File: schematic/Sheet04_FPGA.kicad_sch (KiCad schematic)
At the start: 6 parts

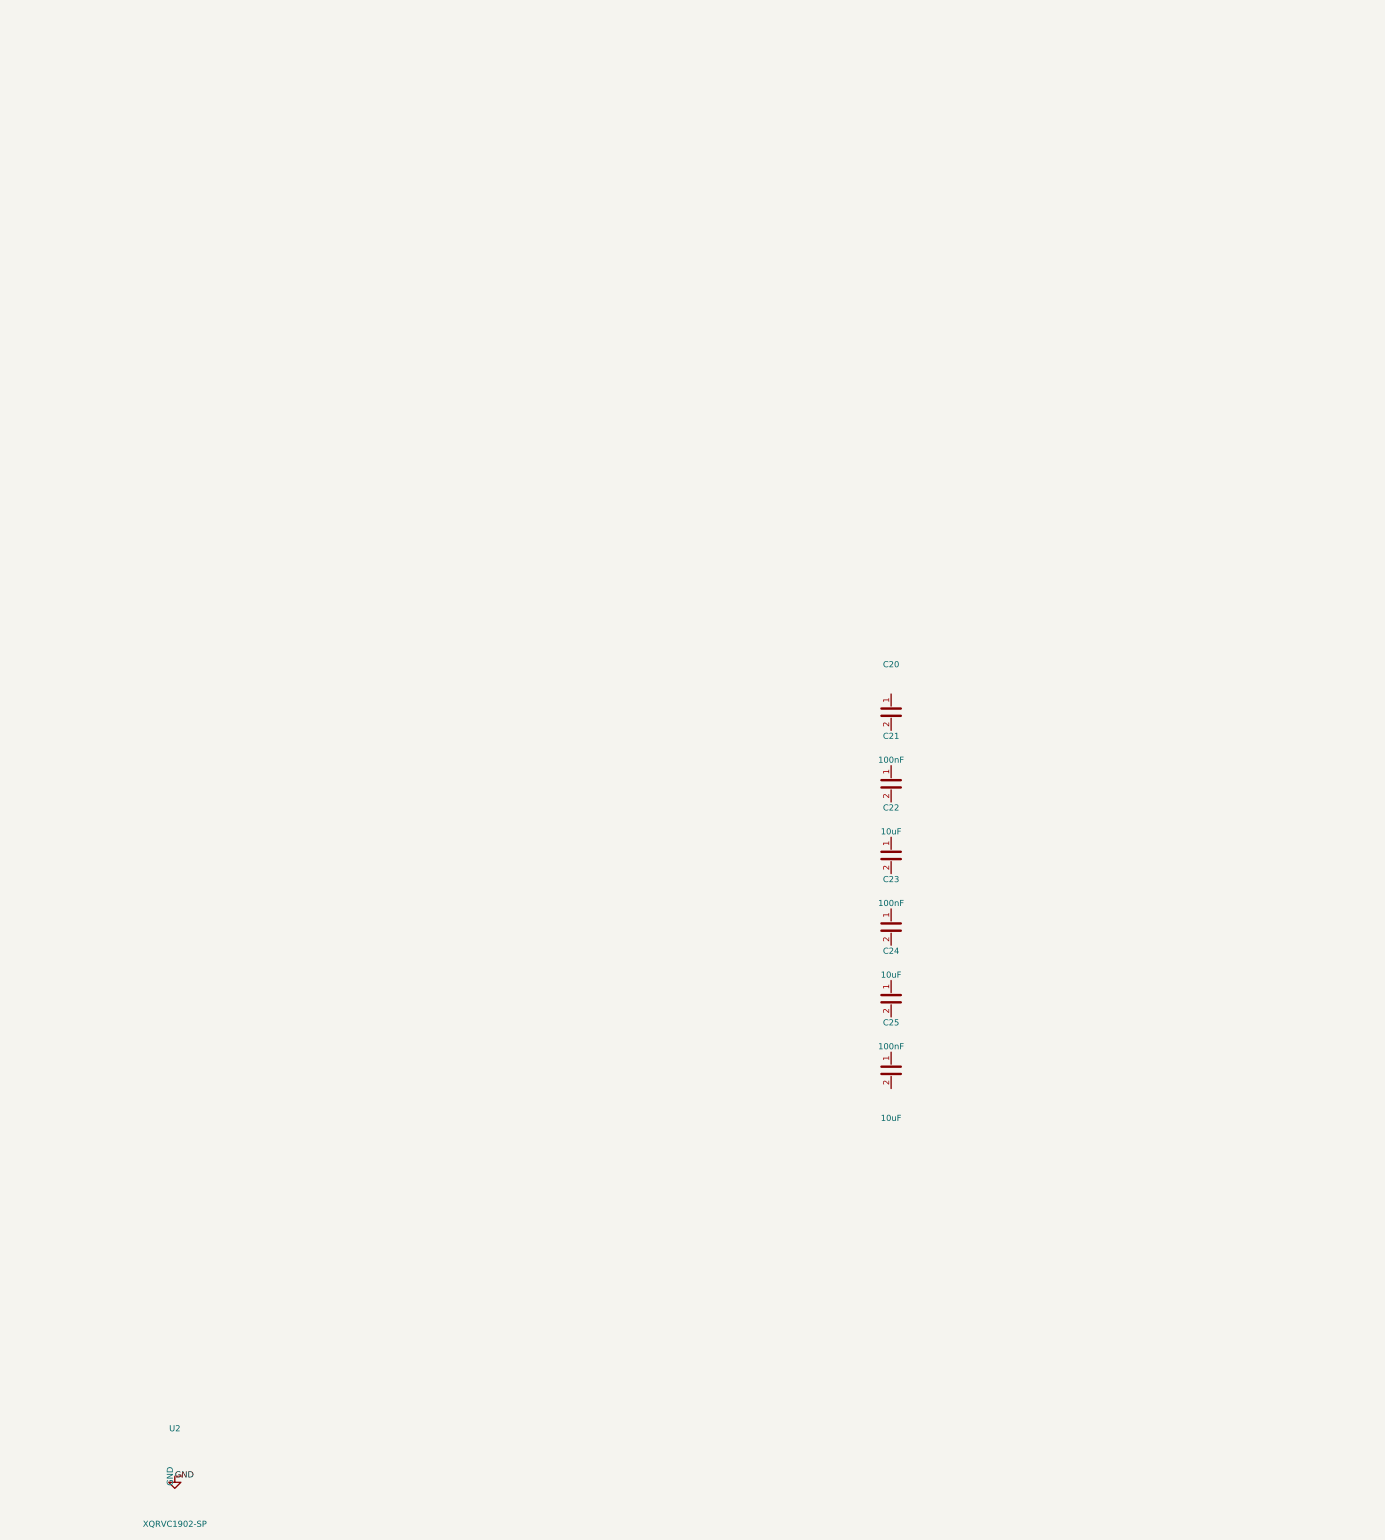
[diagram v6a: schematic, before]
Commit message: fix: isolate ISL70003ASEH buck pins, fix LMX_SYNC collision, NC pins, connector pin names
- ISL70003ASEH pins now use ref prefix (U6_LX1 vs U7_LX1) to prevent shorts
- Buck SYNC pins separated from LMX_SYNC (power sync ≠ PLL sync)
- NC pins properly skipped (unconnected)
- Connector PIN_1..PIN_6 use ref prefix (J1_PIN_1 vs J2_PIN_1)
- Fixed annotation warnings in Sheet13 (C_dev→C125, R_dev→R74, U_TPS7H→U14)
- Regenerated all PDFs and SVGs
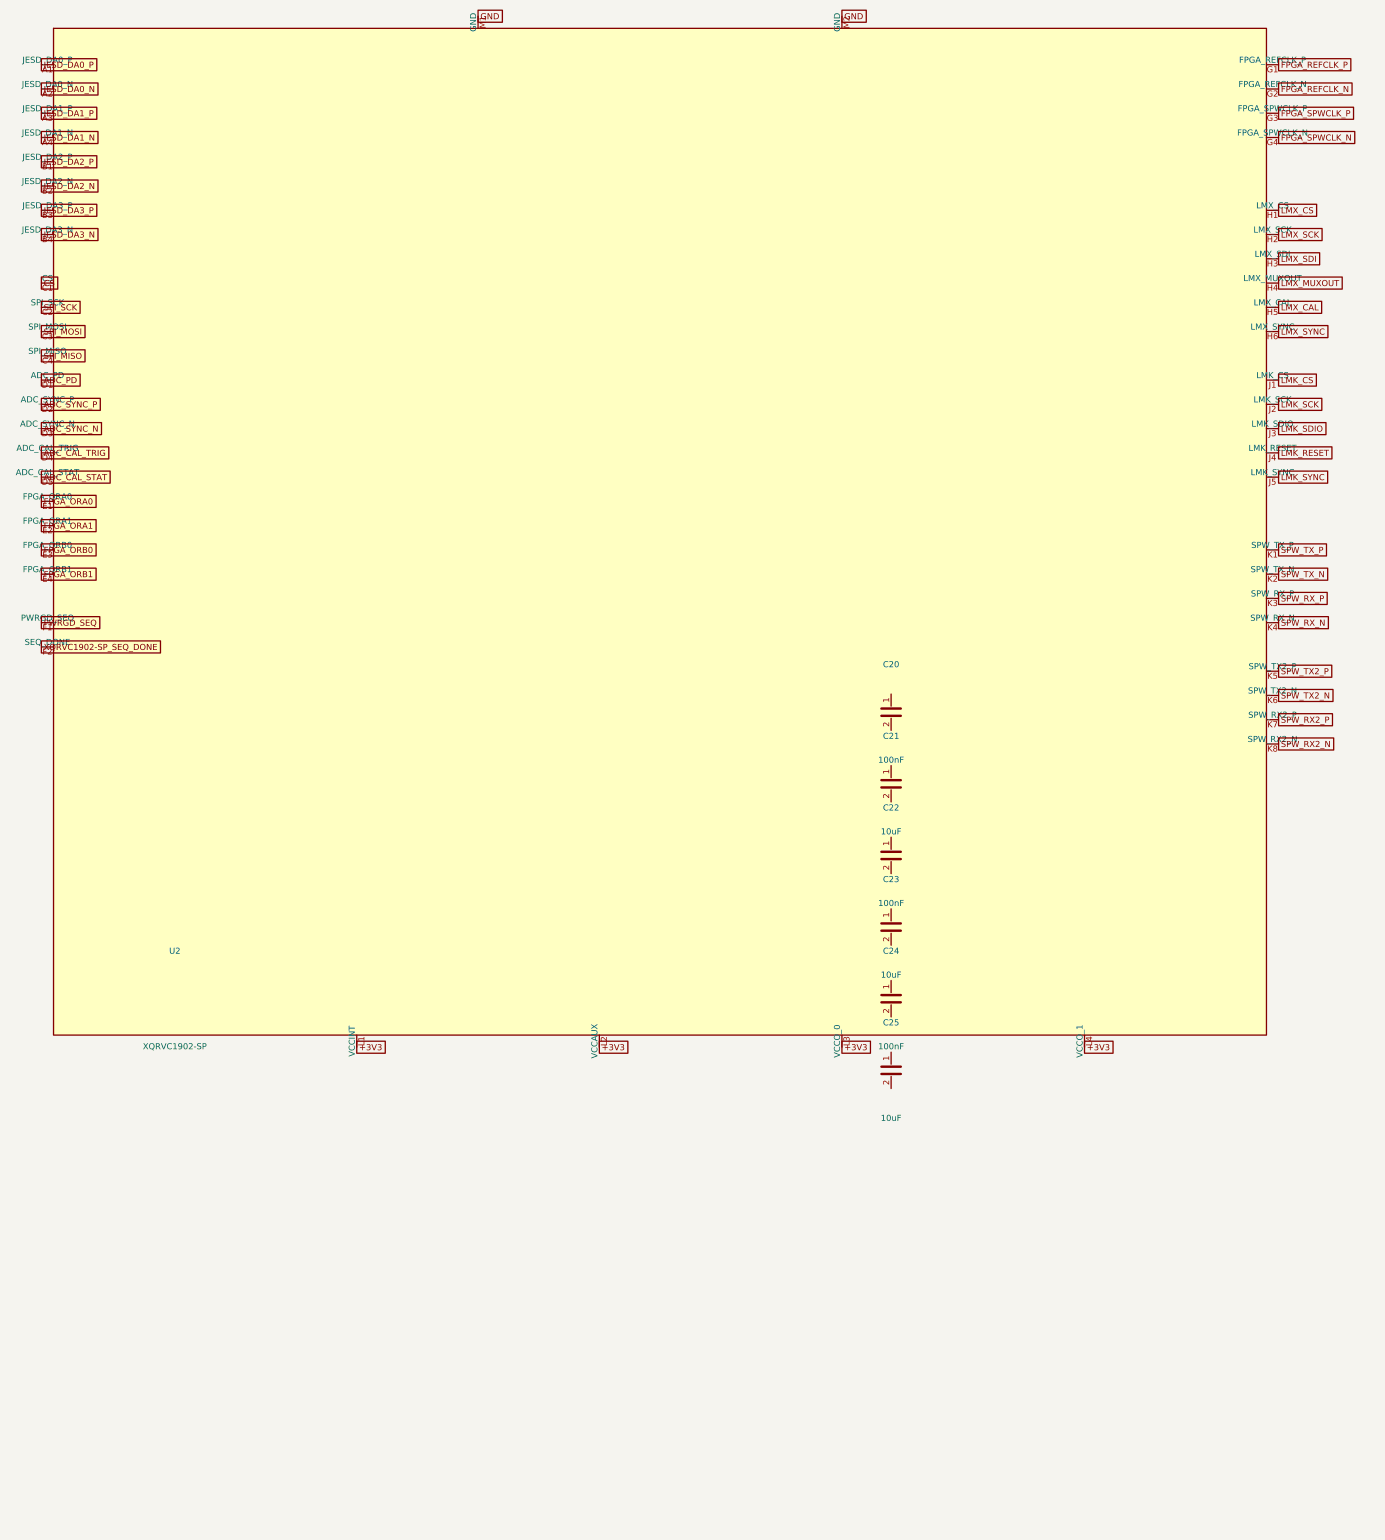
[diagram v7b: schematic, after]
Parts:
- added U2: XQRVC1902-SP, symbol Custom:XQRVC1902-SP
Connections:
- net GND: now also U2.M1 (GND), U2.M2 (GND)
- new net +3V3: U2.L1 (VCCINT), U2.L2 (VCCAUX), U2.L3 (VCCO_0), U2.L4 (VCCO_1)
- new net ADC_CAL_STAT: U2.D5 (ADC_CAL_STAT)
- new net ADC_CAL_TRIG: U2.D4 (ADC_CAL_TRIG)
- new net ADC_PD: U2.D1 (ADC_PD)
- new net ADC_SYNC_N: U2.D3 (ADC_SYNC_N)
- new net ADC_SYNC_P: U2.D2 (ADC_SYNC_P)
- new net CS: U2.C1 (CS)
- new net FPGA_ORA0: U2.E1 (FPGA_ORA0)
- new net FPGA_ORA1: U2.E2 (FPGA_ORA1)
- new net FPGA_ORB0: U2.E3 (FPGA_ORB0)
- new net FPGA_ORB1: U2.E4 (FPGA_ORB1)
- new net FPGA_REFCLK_N: U2.G2 (FPGA_REFCLK_N)
- new net FPGA_REFCLK_P: U2.G1 (FPGA_REFCLK_P)
- new net FPGA_SPWCLK_N: U2.G4 (FPGA_SPWCLK_N)
- new net FPGA_SPWCLK_P: U2.G3 (FPGA_SPWCLK_P)
- new net JESD_DA0_N: U2.A2 (JESD_DA0_N)
- new net JESD_DA0_P: U2.A1 (JESD_DA0_P)
- new net JESD_DA1_N: U2.A4 (JESD_DA1_N)
- new net JESD_DA1_P: U2.A3 (JESD_DA1_P)
- new net JESD_DA2_N: U2.B2 (JESD_DA2_N)
- new net JESD_DA2_P: U2.B1 (JESD_DA2_P)
- new net JESD_DA3_N: U2.B4 (JESD_DA3_N)
- new net JESD_DA3_P: U2.B3 (JESD_DA3_P)
- new net LMK_CS: U2.J1 (LMK_CS)
- new net LMK_RESET: U2.J4 (LMK_RESET)
- new net LMK_SCK: U2.J2 (LMK_SCK)
- new net LMK_SDIO: U2.J3 (LMK_SDIO)
- new net LMK_SYNC: U2.J5 (LMK_SYNC)
- new net LMX_CAL: U2.H5 (LMX_CAL)
- new net LMX_CS: U2.H1 (LMX_CS)
- new net LMX_MUXOUT: U2.H4 (LMX_MUXOUT)
- new net LMX_SCK: U2.H2 (LMX_SCK)
- new net LMX_SDI: U2.H3 (LMX_SDI)
- new net LMX_SYNC: U2.H6 (LMX_SYNC)
- new net PWRGD_SEQ: U2.F1 (PWRGD_SEQ)
- new net SPI_MISO: U2.C4 (SPI_MISO)
- new net SPI_MOSI: U2.C3 (SPI_MOSI)
- new net SPI_SCK: U2.C2 (SPI_SCK)
- new net SPW_RX2_N: U2.K8 (SPW_RX2_N)
- new net SPW_RX2_P: U2.K7 (SPW_RX2_P)
- new net SPW_RX_N: U2.K4 (SPW_RX_N)
- new net SPW_RX_P: U2.K3 (SPW_RX_P)
- new net SPW_TX2_N: U2.K6 (SPW_TX2_N)
- new net SPW_TX2_P: U2.K5 (SPW_TX2_P)
- new net SPW_TX_N: U2.K2 (SPW_TX_N)
- new net SPW_TX_P: U2.K1 (SPW_TX_P)
- new net XQRVC1902-SP_SEQ_DONE: U2.F2 (SEQ_DONE)
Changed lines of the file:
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@@
     (rev "1.0")
   )
-  (symbol (lib_id "power:GND") (at 200 200 0) (unit 1)
+  (symbol (lib_id "Custom:XQRVC1902-SP") (at 200 100 0) (unit 1)
     (in_bom yes) (on_board yes)
-    (property "Reference" "U2" (at 200 190 0) (effects (font (size 1.27 1.27))))
-    (property "Value" "XQRVC1902-SP" (at 200 210 0) (effects (font (size 1.27 1.27))))
-    (property "Footprint" "" (at 200 200 0) (effects (font (size 1.27 1.27)) hide))
+    (property "Reference" "U2" (at 200 90 0) (effects (font (size 1.27 1.27))))
+    (property "Value" "XQRVC1902-SP" (at 200 110 0) (effects (font (size 1.27 1.27))))
+    (property "Footprint" "" (at 0 0 0) (effects (font (size 1.27 1.27)) hide))
   )
-                                                                                                  (symbol (lib_id "Device:C") (at 350 40 0) (unit 1)
+  (symbol (lib_id "Device:C") (at 350 40 0) (unit 1)
     (in_bom yes) (on_board yes)
     (property "Reference" "C20" (at 350 30 0) (effects (font (size 1.27 1.27))))
@@
     (pin "2")
   )
-  (label "GND" (at 200.0000 200.0000 0) (effects (font (size 1.27 1.27))))
+  (global_label "JESD_DA0_P" (at 172.0600 -95.5800 0) (effects (font (size 1.27 1.27))))
+  (global_label "JESD_DA0_N" (at 172.0600 -90.5000 0) (effects (font (size 1.27 1.27))))
+  (global_label "JESD_DA1_P" (at 172.0600 -85.4200 0) (effects (font (size 1.27 1.27))))
+  (global_label "JESD_DA1_N" (at 172.0600 -80.3400 0) (effects (font (size 1.27 1.27))))
+  (global_label "JESD_DA2_P" (at 172.0600 -75.2600 0) (effects (font (size 1.27 1.27))))
+  (global_label "JESD_DA2_N" (at 172.0600 -70.1800 0) (effects (font (size 1.27 1.27))))
+  (global_label "JESD_DA3_P" (at 172.0600 -65.1000 0) (effects (font (size 1.27 1.27))))
+  (global_label "JESD_DA3_N" (at 172.0600 -60.0200 0) (effects (font (size 1.27 1.27))))
+  (global_label "CS" (at 172.0600 -49.8600 0) (effects (font (size 1.27 1.27))))
+  (global_label "SPI_SCK" (at 172.0600 -44.7800 0) (effects (font (size 1.27 1.27))))
+  (global_label "SPI_MOSI" (at 172.0600 -39.7000 0) (effects (font (size 1.27 1.27))))
+  (global_label "SPI_MISO" (at 172.0600 -34.6200 0) (effects (font (size 1.27 1.27))))
+  (global_label "ADC_PD" (at 172.0600 -29.5400 0) (effects (font (size 1.27 1.27))))
+  (global_label "ADC_SYNC_P" (at 172.0600 -24.4600 0) (effects (font (size 1.27 1.27))))
+  (global_label "ADC_SYNC_N" (at 172.0600 -19.3800 0) (effects (font (size 1.27 1.27))))
+  (global_label "ADC_CAL_TRIG" (at 172.0600 -14.3000 0) (effects (font (size 1.27 1.27))))
+  (global_label "ADC_CAL_STAT" (at 172.0600 -9.2200 0) (effects (font (size 1.27 1.27))))
+  (global_label "FPGA_ORA0" (at 172.0600 -4.1400 0) (effects (font (size 1.27 1.27))))
+  (global_label "FPGA_ORA1" (at 172.0600 0.9400 0) (effects (font (size 1.27 1.27))))
+  (global_label "FPGA_ORB0" (at 172.0600 6.0200 0) (effects (font (size 1.27 1.27))))
+  (global_label "FPGA_ORB1" (at 172.0600 11.1000 0) (effects (font (size 1.27 1.27))))
+  (global_label "PWRGD_SEQ" (at 172.0600 21.2600 0) (effects (font (size 1.27 1.27))))
+  (global_label "XQRVC1902-SP_SEQ_DONE" (at 172.0600 26.3400 0) (effects (font (size 1.27 1.27))))
+  (global_label "FPGA_REFCLK_P" (at 431.1400 -95.5800 0) (effects (font (size 1.27 1.27))))
+  (global_label "FPGA_REFCLK_N" (at 431.1400 -90.5000 0) (effects (font (size 1.27 1.27))))
+  (global_label "FPGA_SPWCLK_P" (at 431.1400 -85.4200 0) (effects (font (size 1.27 1.27))))
+  (global_label "FPGA_SPWCLK_N" (at 431.1400 -80.3400 0) (effects (font (size 1.27 1.27))))
+  (global_label "LMX_CS" (at 431.1400 -65.1000 0) (effects (font (size 1.27 1.27))))
+  (global_label "LMX_SCK" (at 431.1400 -60.0200 0) (effects (font (size 1.27 1.27))))
+  (global_label "LMX_SDI" (at 431.1400 -54.9400 0) (effects (font (size 1.27 1.27))))
+  (global_label "LMX_MUXOUT" (at 431.1400 -49.8600 0) (effects (font (size 1.27 1.27))))
+  (global_label "LMX_CAL" (at 431.1400 -44.7800 0) (effects (font (size 1.27 1.27))))
+  (global_label "LMX_SYNC" (at 431.1400 -39.7000 0) (effects (font (size 1.27 1.27))))
+  (global_label "LMK_CS" (at 431.1400 -29.5400 0) (effects (font (size 1.27 1.27))))
+  (global_label "LMK_SCK" (at 431.1400 -24.4600 0) (effects (font (size 1.27 1.27))))
+  (global_label "LMK_SDIO" (at 431.1400 -19.3800 0) (effects (font (size 1.27 1.27))))
+  (global_label "LMK_RESET" (at 431.1400 -14.3000 0) (effects (font (size 1.27 1.27))))
+  (global_label "LMK_SYNC" (at 431.1400 -9.2200 0) (effects (font (size 1.27 1.27))))
+  (global_label "SPW_TX_P" (at 431.1400 6.0200 0) (effects (font (size 1.27 1.27))))
+  (global_label "SPW_TX_N" (at 431.1400 11.1000 0) (effects (font (size 1.27 1.27))))
+  (global_label "SPW_RX_P" (at 431.1400 16.1800 0) (effects (font (size 1.27 1.27))))
+  (global_label "SPW_RX_N" (at 431.1400 21.2600 0) (effects (font (size 1.27 1.27))))
+  (global_label "SPW_TX2_P" (at 431.1400 31.4200 0) (effects (font (size 1.27 1.27))))
+  (global_label "SPW_TX2_N" (at 431.1400 36.5000 0) (effects (font (size 1.27 1.27))))
+  (global_label "SPW_RX2_P" (at 431.1400 41.5800 0) (effects (font (size 1.27 1.27))))
+  (global_label "SPW_RX2_N" (at 431.1400 46.6600 0) (effects (font (size 1.27 1.27))))
+  (global_label "+3V3" (at 238.1000 110.1600 0) (effects (font (size 1.27 1.27))))
+  (global_label "+3V3" (at 288.9000 110.1600 0) (effects (font (size 1.27 1.27))))
+  (global_label "+3V3" (at 339.7000 110.1600 0) (effects (font (size 1.27 1.27))))
+  (global_label "+3V3" (at 390.5000 110.1600 0) (effects (font (size 1.27 1.27))))
+  (global_label "GND" (at 263.5000 -105.7400 0) (effects (font (size 1.27 1.27))))
+  (global_label "GND" (at 339.7000 -105.7400 0) (effects (font (size 1.27 1.27))))
   (sheet_instances (path "/" (page "1")))
 )

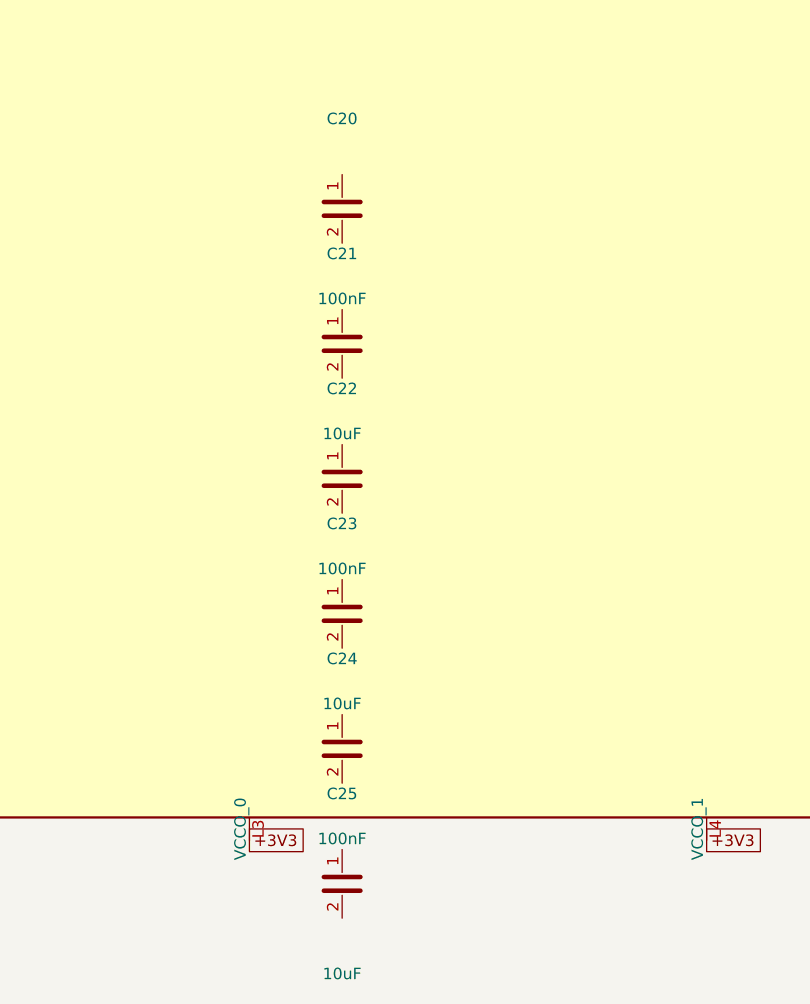
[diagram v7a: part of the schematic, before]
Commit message: feat: connect ALL passive components and fix clock routing
- Added PASSIVE_TOPOLOGY dict mapping 139 passives to their nets
- Passive pin endpoints now get global_labels (was 0 connected, now 138)
- R38 intentionally GND-GND (RECAL_EN pull-down)
- Fixed LMK clock output mapping: CLKout0→ADC_CLK_P, CLKout2→FPGA_REFCLK_P, etc.
- Fixed TPS7H5001-SP SYNC pin collision with LMX_SYNC
- Total connections: 867 pins (up from 641)
- Cross-sheet nets: 52
- Power rails: VIN(33), +3V3(98), GND(228) all with decoupling
- JESD204C: U1↔U2 on 4 lanes ✓
- SPI: U1↔U2↔U3↔U4 ✓
- Clock: LMK→ADC (CLK+SYSREF), LMK→FPGA (REF+SPW) ✓
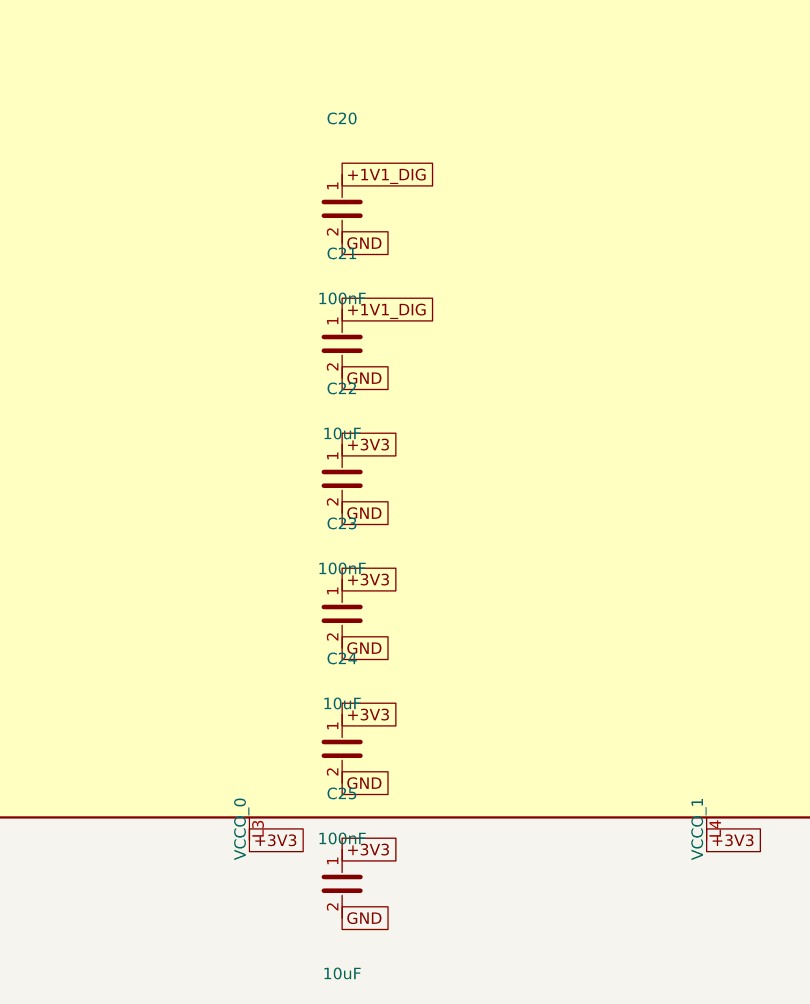
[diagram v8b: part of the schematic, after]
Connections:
- net +3V3: now also C22.1, C23.1, C24.1, C25.1
- net GND: now also C20.2, C21.2, C22.2, C23.2, C24.2, C25.2
- net +1V1_DIG: now reaches C20.1
- net +1V1_DIG: now also C21.1
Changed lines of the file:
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@@
   (global_label "GND" (at 263.5000 -105.7400 0) (effects (font (size 1.27 1.27))))
   (global_label "GND" (at 339.7000 -105.7400 0) (effects (font (size 1.27 1.27))))
+  (global_label "+1V1_DIG" (at 350.0000 36.1900 0) (effects (font (size 1.27 1.27))))
+  (global_label "GND" (at 350.0000 43.8100 0) (effects (font (size 1.27 1.27))))
+  (global_label "+1V1_DIG" (at 350.0000 51.1900 0) (effects (font (size 1.27 1.27))))
+  (global_label "GND" (at 350.0000 58.8100 0) (effects (font (size 1.27 1.27))))
+  (global_label "+3V3" (at 350.0000 66.1900 0) (effects (font (size 1.27 1.27))))
+  (global_label "GND" (at 350.0000 73.8100 0) (effects (font (size 1.27 1.27))))
+  (global_label "+3V3" (at 350.0000 81.1900 0) (effects (font (size 1.27 1.27))))
+  (global_label "GND" (at 350.0000 88.8100 0) (effects (font (size 1.27 1.27))))
+  (global_label "+3V3" (at 350.0000 96.1900 0) (effects (font (size 1.27 1.27))))
+  (global_label "GND" (at 350.0000 103.8100 0) (effects (font (size 1.27 1.27))))
+  (global_label "+3V3" (at 350.0000 111.1900 0) (effects (font (size 1.27 1.27))))
+  (global_label "GND" (at 350.0000 118.8100 0) (effects (font (size 1.27 1.27))))
   (sheet_instances (path "/" (page "1")))
 )
